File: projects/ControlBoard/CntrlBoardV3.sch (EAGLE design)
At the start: 21 parts, among them J9 M50-3600542

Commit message: Continued Control Board and library updates.
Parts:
- added C10, C11, C12, C13: 10uF, BrownSpaceEngineering:CAP0805
- added C14, C15, C18, C19, C20, C21: 0.1uF, BrownSpaceEngineering:CAP0805
- added C16: 4.7uF, BrownSpaceEngineering:CAP0805
- added C17: 22uF, BrownSpaceEngineering:CAP0805
- added L2: 2.2uH, resistor:L-USL3225M
- added L3: 3.3uH, resistor:L-USL3225M
- added R10, R9: 100R, BrownSpaceEngineering:RES0805
- added R11, R12, R13: 10K, BrownSpaceEngineering:RES0805
- added U$2: MPU9250, CNTRL_BOARD:MPU9250
- added U$3: HMC5883L, CNTRL_BOARD:HMC5883L
- added U$4: TPS63001, CNTRL_BOARD:TPS6300X
- added U$5: TPS63002, CNTRL_BOARD:TPS6300X
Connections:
- new net +5V: C13.P$1, U$5.FB, U$5.VOUT
- new net 5V_EN: R11.2, U$5.EN
- new net AD0: R12.1, R13.2, U$2.AD0
- new net N$10: C15.P$1, R10.1, U$5.PS/SYNC, U$5.VINA
- new net N$11: C16.P$1, U$3.C1
- new net N$13: C20.P$1, U$2.REGOUT
- new net N$14: C17.P$2, U$3.SETC
- new net N$15: C17.P$1, U$3.SETP
- new net N$5: L2.1, U$4.L1
- new net N$6: L2.2, U$4.L2
- new net N$7: L3.1, U$5.L1
- new net N$8: L3.2, U$5.L2
- new net N$9: C14.P$1, R9.1, U$4.EN, U$4.PS/SYNC, U$4.VINA
- new net VIN: C10.P$1, C11.P$1, R10.2, R9.2, U$4.VIN, U$5.VIN
- net +3V3: now also C12.P$1, C18.P$1, C19.P$1, C21.P$1, R12.2, U$2.RESV@1, U$2.VDD, U$2.VDDIO, U$3.S1, U$3.VDD, U$3.VDDIO, U$4.FB, U$4.VOUT
- net GND: now also C10.P$2, C11.P$2, C12.P$2, C13.P$2, C14.P$2, C15.P$2, C16.P$2, C18.P$2, C19.P$2, C20.P$2, C21.P$2, R11.1, R13.1, U$2.FSYNC, U$2.GND, U$2.RESV@3, U$3.GND@1, U$3.GND@2, U$4.GND, U$4.PGND, U$5.GND, U$5.PGND
- net SCL: now also U$2.SCL, U$3.SCL
- net SDA: now also U$2.SDA, U$3.SDA
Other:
- note added: "3V3 Regulator"
- note added: "5V Regulator"
- note added: "Only connect either R12 OR R13"

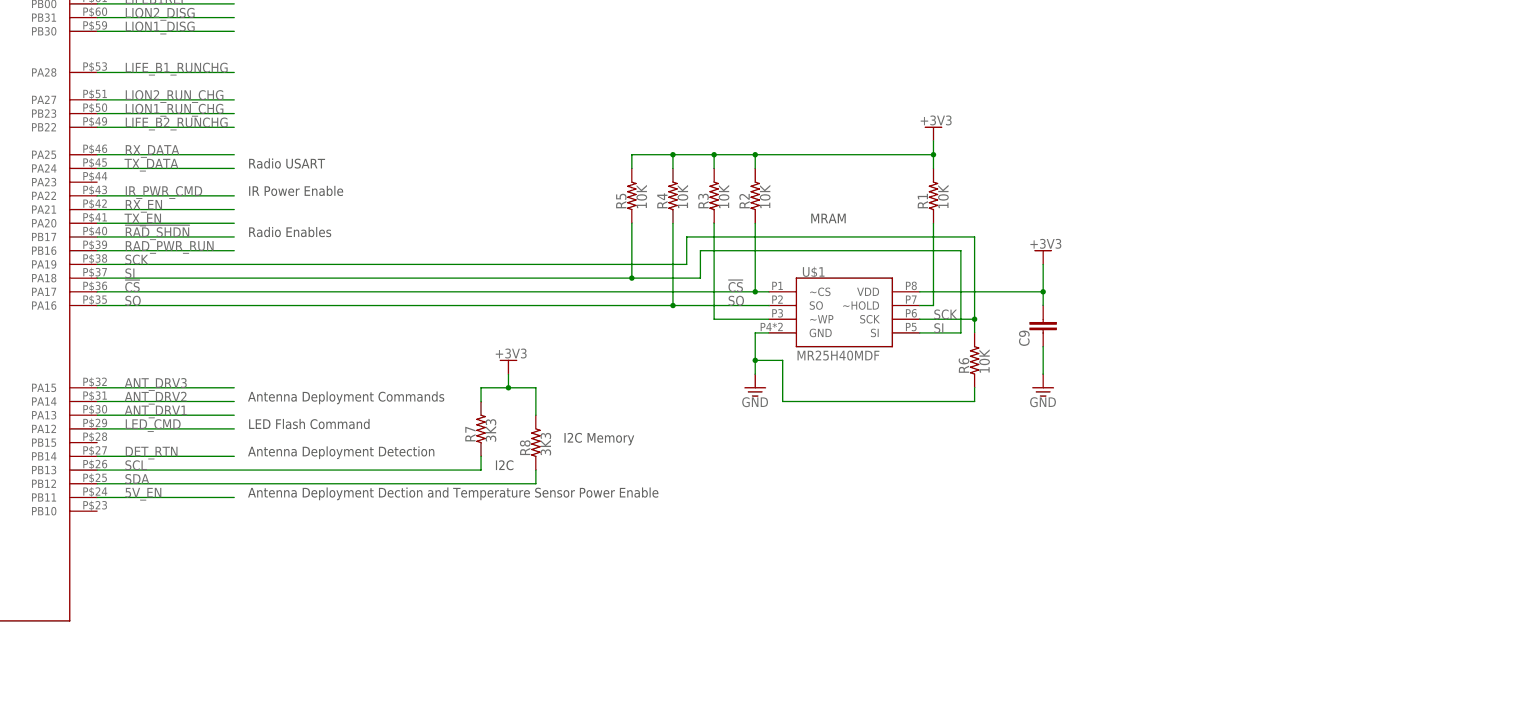
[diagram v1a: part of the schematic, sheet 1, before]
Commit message: Added external memories and library updates.
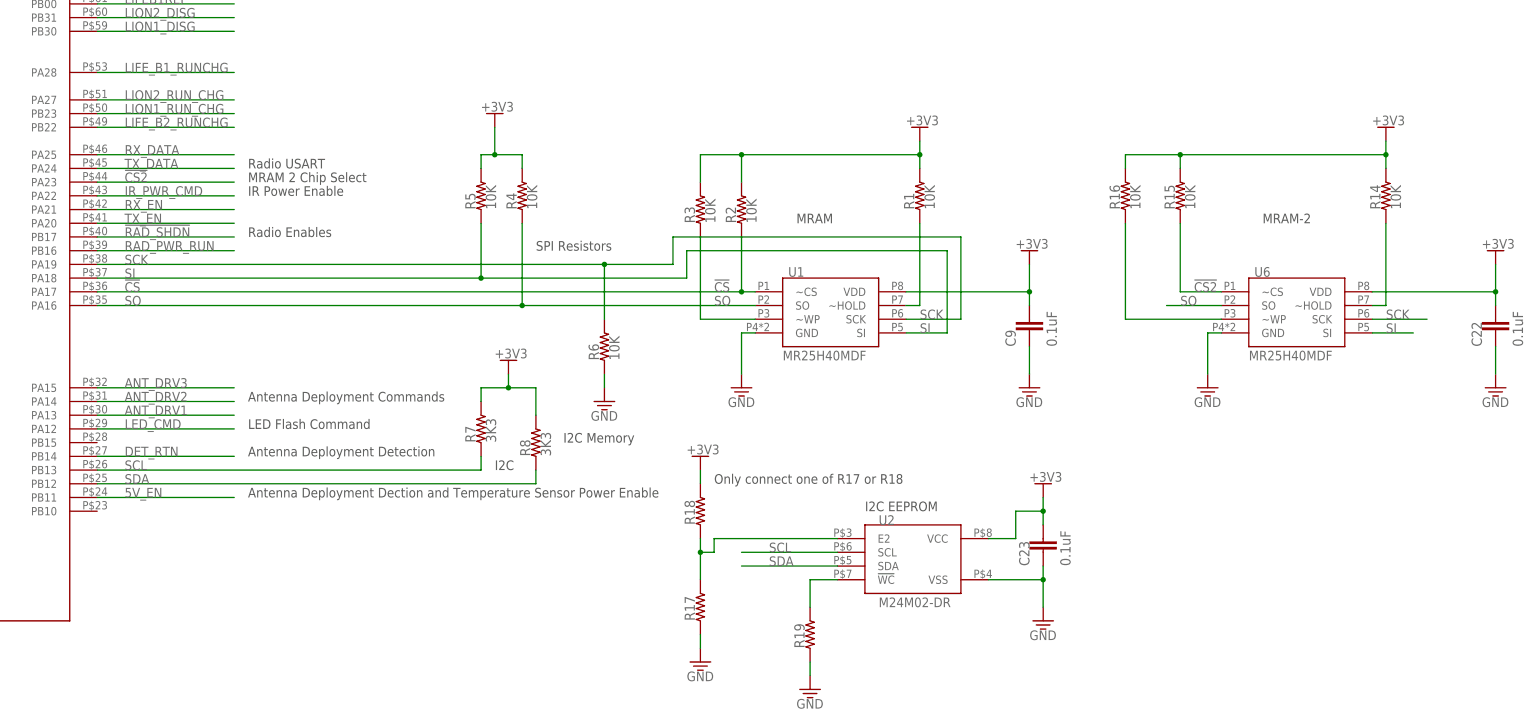
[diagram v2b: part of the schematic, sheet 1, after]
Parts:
- removed U$1: MR25H40MDF, BrownSpaceEngineering:MR2XHXX
- added C22, C23: 0.1uF, BrownSpaceEngineering:CAP0805
- added R14, R15, R16: 10K, BrownSpaceEngineering:RES0805
- added R17, R18, R19: (no value), BrownSpaceEngineering:RES0805
- added U1, U6: MR25H40MDF, BrownSpaceEngineering:MR2XHXX
- added U2: M24M02-DR, BrownSpaceEngineering:M24M02-DR
- C9: value (none) -> 0.1uF
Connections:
- new net !CS2!: R15.1, U6.~CS, UC1.PA23
- new net N$12: R16.1, U6.~WP
- new net N$16: R14.1, U6.~HOLD
- new net N$17: R17.2, R18.1, U2.E2
- new net N$18: R19.2, U2.!WC!
- net !CS!: now also U1.~CS; no longer U$1.~CS
- net +3V3: now also C22.P$1, C23.P$1, R14.2, R15.2, R16.2, R18.2, U1.VDD, U2.VCC, U6.VDD; no longer U$1.VDD
- net GND: now also C22.P$2, C23.P$2, R17.1, R19.1, U1.GND, U2.VSS, U6.GND; no longer U$1.GND
- net N$3: now also U1.~WP; no longer U$1.~WP
- net N$4: now also U1.~HOLD; no longer U$1.~HOLD
- net SCK: now also U1.SCK, U6.SCK; no longer U$1.SCK
- net SCL: now also U2.SCL
- net SDA: now also U2.SDA
- net SI: now also U1.SI, U6.SI; no longer U$1.SI
- net SO: now also U1.SO, U6.SO; no longer U$1.SO
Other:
- note added: "I2C EEPROM"
- note added: "MRAM 2 Chip Select"
- note added: "MRAM-2"
- note added: "Only connect one of R17 or R18"
- note added: "SPI Resistors"
- moved on the sheet: C9, R1, R2, R3, R4, R5, R6

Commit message: Continued Control Board Updates and library updates. Added Multiplexers, Opamps, Diodes, multiplexing circuitry, instrumentation circuitry, and remote ADC.
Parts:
- added C24, C25, C29, C30, C31, C32, C33, C34: 0.1uF, BrownSpaceEngineering:CAP0805
- added C26: 1uF, BrownSpaceEngineering:CAP0805
- added C27, C28: 0.01uF, BrownSpaceEngineering:CAP0805
- added D1, D2: 1N4148SOD-523F, BrownSpaceEngineering:1N4148SOD-523F
- added J7: M83-LMT1M2N36, BrownSpaceEngineering:M83-LMT1M2N36
- added J8: M80-5101005, BrownSpaceEngineering:M80-5101005
- added M1: AON7522E, BrownSpaceEngineering:AON7522E
- added M2: SI4427BDY-T1-E3CT-ND, CNTRL_BOARD:POWERPMOS
- added R20: 0R, BrownSpaceEngineering:RES0805
- added R21, R41: 1K, BrownSpaceEngineering:RES0805
- added R22: 100R, BrownSpaceEngineering:RES0805
- added R23, R35, R37: 91K, BrownSpaceEngineering:RES0805
- added R24, R25, R26, R27, R28, R29, R30, R31, R32, R33, R34, R38: 10K, BrownSpaceEngineering:RES0805
- added R36: 100K, BrownSpaceEngineering:RES0805
- added R39: 3.3K, BrownSpaceEngineering:RES0805
- added R40: 220, BrownSpaceEngineering:RES0805
- added U10: LT6015, BrownSpaceEngineering:LT6015
- added U11: LT6016, BrownSpaceEngineering:LT6016
- added U3, U4: SN74LVC1G125, BrownSpaceEngineering:SN74LVC1G125
- added U5: (no value), BrownSpaceEngineering:TLC555
- added U7: AD7991-1, BrownSpaceEngineering:AD7991-1
- added U8, U9: LTC1380-GN, BrownSpaceEngineering:LTC1380-GN
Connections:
- new net !LED_CMD!: C28.P$1, R25.2
- new net !RAD_SHDN!: J8.5
- new net 3V3REF: U7.VIN3/REF
- new net 3V6_REF: J8.8, U7.VIN0
- new net 3V6_SNS: J8.3, U7.VIN1
- new net 5VREF: U7.VIN2
- new net A0_0: R26.1, R28.2, U8.A0
- new net A0_1: R30.1, R32.2, U9.A0
- new net A1_0: R27.1, R29.2, U8.A1
- new net A1_1: R31.1, R33.2, U9.A1
- new net IRVDD: M2.D
- new net IR_PWR_CMD: M1.G, R21.1
- new net L1_TEMP: J7.P$1, U8.S4
- new net L2_TEMP: U8.S5
- new net LED1TEMP: U8.S0
- new net LED2TEMP: U8.S1
- new net LED3TEMP: U8.S2
- new net LED4TEMP: U8.S3
- new net LED_SDHN: U5.OUT
- new net LF1_TEMP: U8.S6
- new net LF3REF: J7.P$19
- new net LF3_TEMP: U8.S7
- new net LF4REF: J7.P$20
- new net N$19: R34.2, R35.2, U10.+
- new net N$20: C26.P$1, R23.2, U5.DISG, U5.THRSH
- new net N$22: M1.D, M2.G, R22.1
- new net N$23: C27.P$1, U5.CV
- new net N$24: R38.2, R39.2, R40.1
- new net N$25: R37.2, R38.1, U10.-
- new net N$27: R36.2, R37.1, U10.OUT
- new net N$29: J7.P$21
- new net N$30: J7.P$22
- new net N$31: J7.P$23
- new net N$32: J7.P$24
- new net PD_FLASH: U9.S0
- new net PD_IN: U9.DO
- new net PD_XN: U9.S2
- new net PD_XP: U9.S1
- new net PD_YN: U9.S3
- new net PD_ZN: U9.S5
- new net PD_ZP: U9.S4
- new net RAD_PWR_RUN: J8.7
- new net RX_DATA: R20.1, U3.Y
- new net RX_EN: U3.!OE!
- new net RX_IN: J8.4, R20.2, U3.A
- new net TEMP_IN: R34.1, R41.2, U8.DO
- new net TEMP_OUT: C32.P$1, R36.1
- new net TRIG: C28.P$2, D1.A, R24.2, U5.TRIG
- new net TX_DATA: U4.A
- new net TX_EN: U4.!OE!
- new net TX_OUT: J8.6, U4.Y
- net +3V3: now also C24.P$1, C25.P$1, C29.P$1, C30.P$2, C31.P$2, C33.P$1, C34.P$1, D1.C, M2.S, R22.2, R23.1, R24.1, R25.1, R26.2, R27.2, R30.2, R31.2, R39.1, U10.V+, U11.V+, U3.VCC, U4.VCC, U5.RST, U5.VCC, U7.VDD, U8.VCC, U9.VCC
- net GND: now also C24.P$2, C25.P$2, C26.P$2, C27.P$2, C29.P$2, C30.P$1, C31.P$1, C32.P$2, C33.P$2, C34.P$2, J8.2, J8.9, M1.S, R21.2, R28.1, R29.1, R32.1, R33.1, R35.1, R40.2, R41.1, U10.V-, U11.V-, U3.GND, U4.GND, U5.GND, U7.GND, U8.GND, U8.VEE, U9.GND, U9.VEE
- net SCL: now also U7.SCL, U8.SCL, U9.SCL
- net SDA: now also U7.SDA, U8.SDA, U9.SDA
- net VIN: now also J8.1, J8.10
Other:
- note added: "Hardware Programmable Address. Only solder one of R26 or R28 and R27 or R29."
- note added: "Hardware Programmable Address. Only solder one of R30 or R32 and R31 or R33."
- note added: "IR Power Control"
- note added: "Optional resistor to bypass tri-state"
- note added: "Photodiode Sensor Demux"
- note added: "Temperature Sensor Demux"

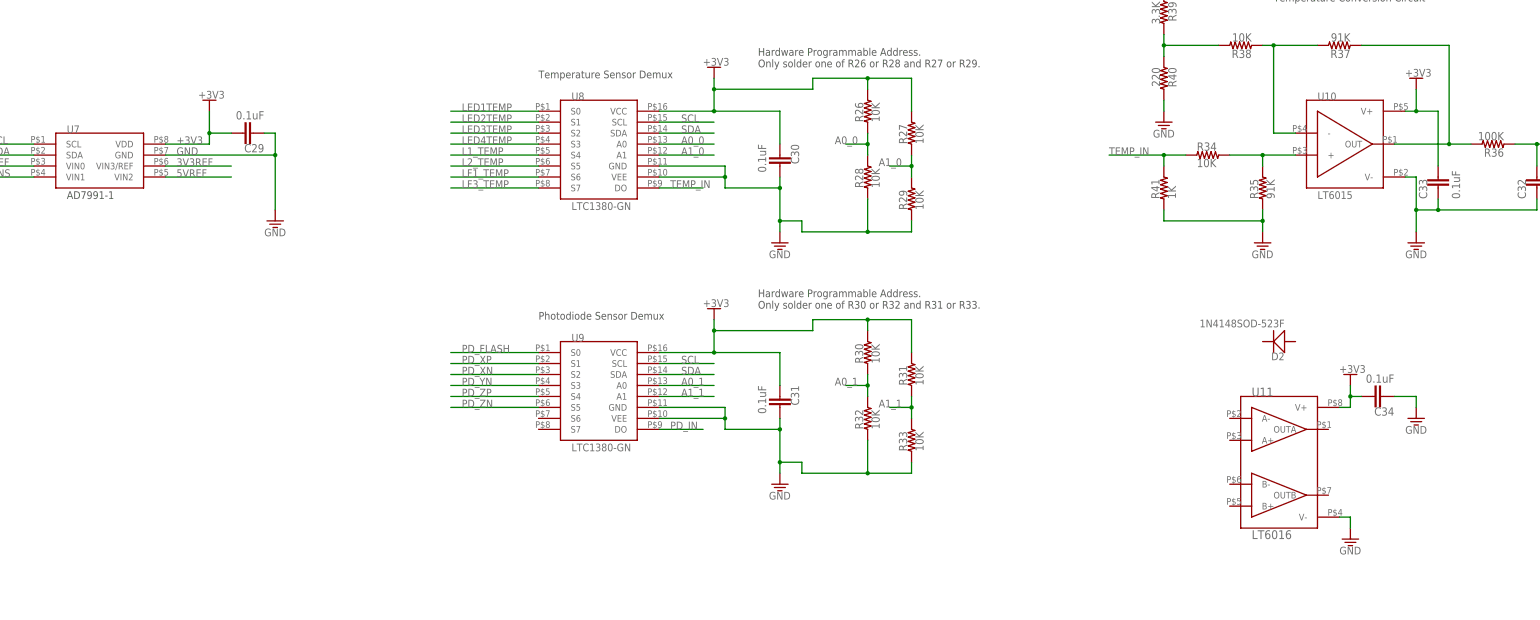
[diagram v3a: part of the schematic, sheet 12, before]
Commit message: Added photodiode instrumentation circuit
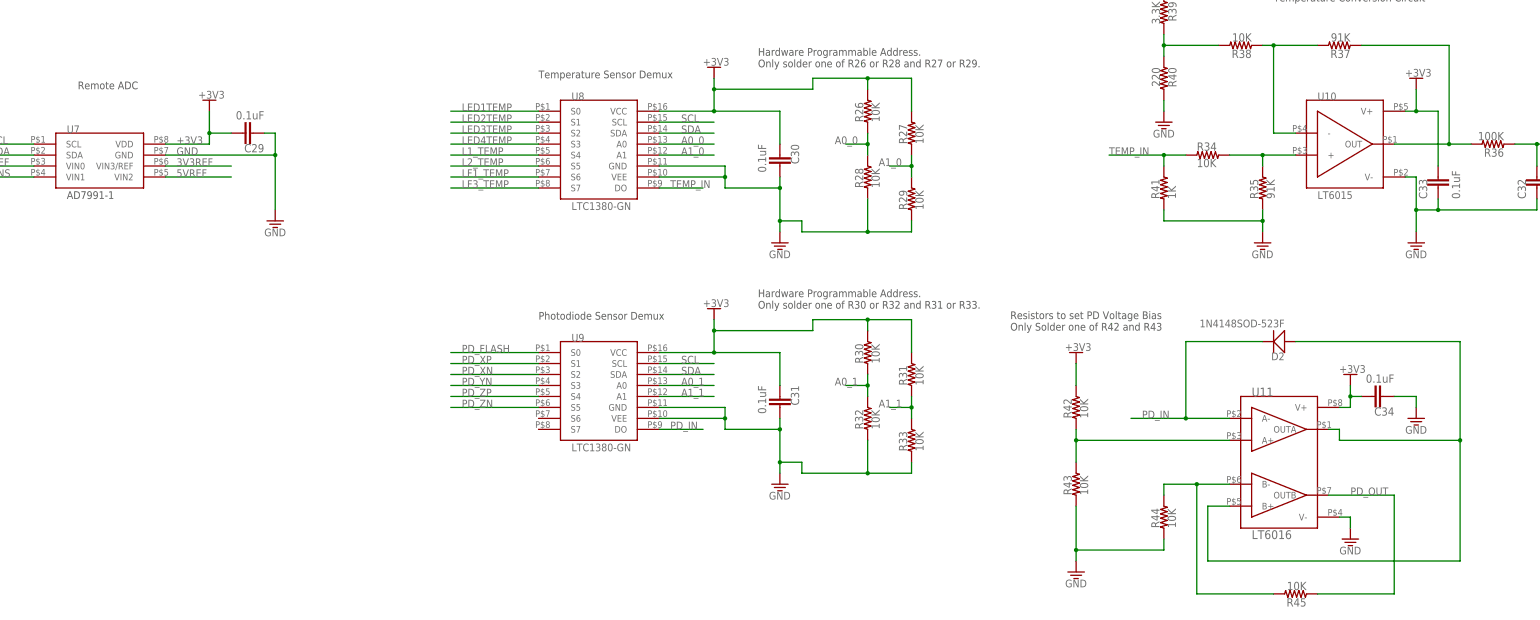
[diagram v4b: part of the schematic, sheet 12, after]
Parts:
- added R42, R43, R44, R45: 10K, BrownSpaceEngineering:RES0805
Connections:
- new net N$33: D2.A, U11.B+, U11.OUTA
- new net N$34: R42.1, R43.2, U11.A+
- new net N$38: R44.2, R45.2, U11.B-
- new net PD_OUT: R45.1, U11.OUTB
- net +3V3: now also R42.2
- net GND: now also R43.1, R44.1
- net PD_IN: now also D2.C, U11.A-
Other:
- note added: "Remote ADC"
- note added: "Resistors to set PD Voltage Bias Only Solder one of R42 and R43"
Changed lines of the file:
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@@
 <part name="C34" library="BrownSpaceEngineering" deviceset="CAP" device="0805" value="0.1uF"/>
 <part name="J7" library="BrownSpaceEngineering" deviceset="M83-LMT1M2N36" device=""/>
+<part name="R42" library="BrownSpaceEngineering" deviceset="RES" device="0805" value="10K"/>
+<part name="R43" library="BrownSpaceEngineering" deviceset="RES" device="0805" value="10K"/>
+<part name="+3V25" library="supply1" deviceset="+3V3" device=""/>
+<part name="GND31" library="supply1" deviceset="GND" device=""/>
+<part name="R44" library="BrownSpaceEngineering" deviceset="RES" device="0805" value="10K"/>
+<part name="R45" library="BrownSpaceEngineering" deviceset="RES" device="0805" value="10K"/>
 </parts>
 <sheets>
@@
 </segment>
 </net>
-<net name="TEMP-OUT" class="0">
+<net name="TEMP_OUT" class="0">
 <segment>
 <wire x1="-7.62" y1="88.9" x2="-33.02" y2="88.9" width="0.1524" layer="91"/>
@@
 </segment>
 </net>
-<net name="PD-OUT" class="0">
+<net name="PD_OUT" class="0">
 <segment>
 <wire x1="-7.62" y1="86.36" x2="-33.02" y2="86.36" width="0.1524" layer="91"/>
@@
 <text x="116.84" y="5.08" size="1.778" layer="97">Photodiode Sensor Demux</text>
 <text x="287.02" y="78.74" size="1.778" layer="97">Temperature Conversion Circuit</text>
+<text x="226.06" y="2.54" size="1.778" layer="97">Resistors to set PD Voltage Bias
+Only Solder one of R42 and R43</text>
+<text x="10.16" y="58.42" size="1.778" layer="97">Remote ADC</text>
 </plain>
 <instances>
@@
 <instance part="GND30" gate="1" x="320.04" y="-17.78"/>
 <instance part="C34" gate="G$1" x="312.42" y="-12.7" rot="R90"/>
+<instance part="R42" gate="R$1" x="241.3" y="-15.24" rot="R90"/>
+<instance part="R43" gate="R$1" x="241.3" y="-33.02" rot="R90"/>
+<instance part="+3V25" gate="G$1" x="241.3" y="-2.54"/>
+<instance part="GND31" gate="1" x="241.3" y="-53.34"/>
+<instance part="R44" gate="R$1" x="261.62" y="-40.64" rot="R90"/>
+<instance part="R45" gate="R$1" x="292.1" y="-58.42" rot="R180"/>
 </instances>
 <busses>
@@
 <wire x1="304.8" y1="-12.7" x2="307.34" y2="-12.7" width="0.1524" layer="91"/>
 <junction x="304.8" y="-12.7"/>
+</segment>
+<segment>
+<pinref part="R42" gate="R$1" pin="2"/>
+<wire x1="241.3" y1="-10.16" x2="241.3" y2="-5.08" width="0.1524" layer="91"/>
+<pinref part="+3V25" gate="G$1" pin="+3V3"/>
 </segment>
 </net>
@@
 <wire x1="320.04" y1="-15.24" x2="320.04" y2="-12.7" width="0.1524" layer="91"/>
 </segment>
+<segment>
+<pinref part="R43" gate="R$1" pin="1"/>
+<wire x1="241.3" y1="-38.1" x2="241.3" y2="-48.26" width="0.1524" layer="91"/>
+<pinref part="GND31" gate="1" pin="GND"/>
+<pinref part="R44" gate="R$1" pin="1"/>
+<wire x1="241.3" y1="-48.26" x2="241.3" y2="-50.8" width="0.1524" layer="91"/>
+<wire x1="261.62" y1="-45.72" x2="261.62" y2="-48.26" width="0.1524" layer="91"/>
+<wire x1="261.62" y1="-48.26" x2="241.3" y2="-48.26" width="0.1524" layer="91"/>
+<junction x="241.3" y="-48.26"/>
+</segment>
 </net>
 <net name="3V3REF" class="0">
@@
 <wire x1="144.78" y1="-20.32" x2="154.94" y2="-20.32" width="0.1524" layer="91"/>
 <label x="147.32" y="-20.32" size="1.778" layer="95"/>
+</segment>
+<segment>
+<pinref part="U11" gate="G$1" pin="A-"/>
+<wire x1="276.86" y1="-17.78" x2="266.7" y2="-17.78" width="0.1524" layer="91"/>
+<pinref part="D2" gate="G$1" pin="C"/>
+<wire x1="266.7" y1="-17.78" x2="254" y2="-17.78" width="0.1524" layer="91"/>
+<wire x1="284.48" y1="0" x2="266.7" y2="0" width="0.1524" layer="91"/>
+<wire x1="266.7" y1="0" x2="266.7" y2="-17.78" width="0.1524" layer="91"/>
+<junction x="266.7" y="-17.78"/>
+<label x="256.54" y="-17.78" size="1.778" layer="95"/>
 </segment>
 </net>
@@
 </segment>
 </net>
+<net name="N$33" class="0">
+<segment>
+<pinref part="D2" gate="G$1" pin="A"/>
+<wire x1="292.1" y1="0" x2="330.2" y2="0" width="0.1524" layer="91"/>
+<wire x1="330.2" y1="0" x2="330.2" y2="-22.86" width="0.1524" layer="91"/>
+<wire x1="330.2" y1="-22.86" x2="302.26" y2="-22.86" width="0.1524" layer="91"/>
+<wire x1="302.26" y1="-22.86" x2="302.26" y2="-20.32" width="0.1524" layer="91"/>
+<pinref part="U11" gate="G$1" pin="OUTA"/>
+<wire x1="302.26" y1="-20.32" x2="299.72" y2="-20.32" width="0.1524" layer="91"/>
+<pinref part="U11" gate="G$1" pin="B+"/>
+<wire x1="276.86" y1="-38.1" x2="271.78" y2="-38.1" width="0.1524" layer="91"/>
+<wire x1="271.78" y1="-38.1" x2="271.78" y2="-50.8" width="0.1524" layer="91"/>
+<wire x1="271.78" y1="-50.8" x2="330.2" y2="-50.8" width="0.1524" layer="91"/>
+<wire x1="330.2" y1="-50.8" x2="330.2" y2="-22.86" width="0.1524" layer="91"/>
+<junction x="330.2" y="-22.86"/>
+</segment>
+</net>
+<net name="N$34" class="0">
+<segment>
+<pinref part="U11" gate="G$1" pin="A+"/>
+<wire x1="276.86" y1="-22.86" x2="241.3" y2="-22.86" width="0.1524" layer="91"/>
+<pinref part="R42" gate="R$1" pin="1"/>
+<wire x1="241.3" y1="-20.32" x2="241.3" y2="-22.86" width="0.1524" layer="91"/>
+<pinref part="R43" gate="R$1" pin="2"/>
+<wire x1="241.3" y1="-27.94" x2="241.3" y2="-22.86" width="0.1524" layer="91"/>
+<junction x="241.3" y="-22.86"/>
+</segment>
+</net>
+<net name="PD_OUT" class="0">
+<segment>
+<pinref part="U11" gate="G$1" pin="OUTB"/>
+<wire x1="299.72" y1="-35.56" x2="314.96" y2="-35.56" width="0.1524" layer="91"/>
+<pinref part="R45" gate="R$1" pin="1"/>
+<wire x1="297.18" y1="-58.42" x2="314.96" y2="-58.42" width="0.1524" layer="91"/>
+<wire x1="314.96" y1="-58.42" x2="314.96" y2="-35.56" width="0.1524" layer="91"/>
+<label x="304.8" y="-35.56" size="1.778" layer="95"/>
+</segment>
+</net>
+<net name="N$38" class="0">
+<segment>
+<pinref part="U11" gate="G$1" pin="B-"/>
+<pinref part="R44" gate="R$1" pin="2"/>
+<wire x1="276.86" y1="-33.02" x2="269.24" y2="-33.02" width="0.1524" layer="91"/>
+<wire x1="269.24" y1="-33.02" x2="261.62" y2="-33.02" width="0.1524" layer="91"/>
+<wire x1="261.62" y1="-33.02" x2="261.62" y2="-35.56" width="0.1524" layer="91"/>
+<pinref part="R45" gate="R$1" pin="2"/>
+<wire x1="287.02" y1="-58.42" x2="269.24" y2="-58.42" width="0.1524" layer="91"/>
+<wire x1="269.24" y1="-58.42" x2="269.24" y2="-33.02" width="0.1524" layer="91"/>
+<junction x="269.24" y="-33.02"/>
+</segment>
+</net>
